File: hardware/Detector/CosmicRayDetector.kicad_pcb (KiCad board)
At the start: 2 copper layers, 100 x 100 mm, 29 parts, among them J1 USB_B_Micro, J2 Conn_01x01_Female, J3 Conn_01x01_Female, J4 Conn_01x01_Female, J5 Conn_01x01_Female, J6 Conn_01x04, J7 Conn_01x02, U1 HEF4093B

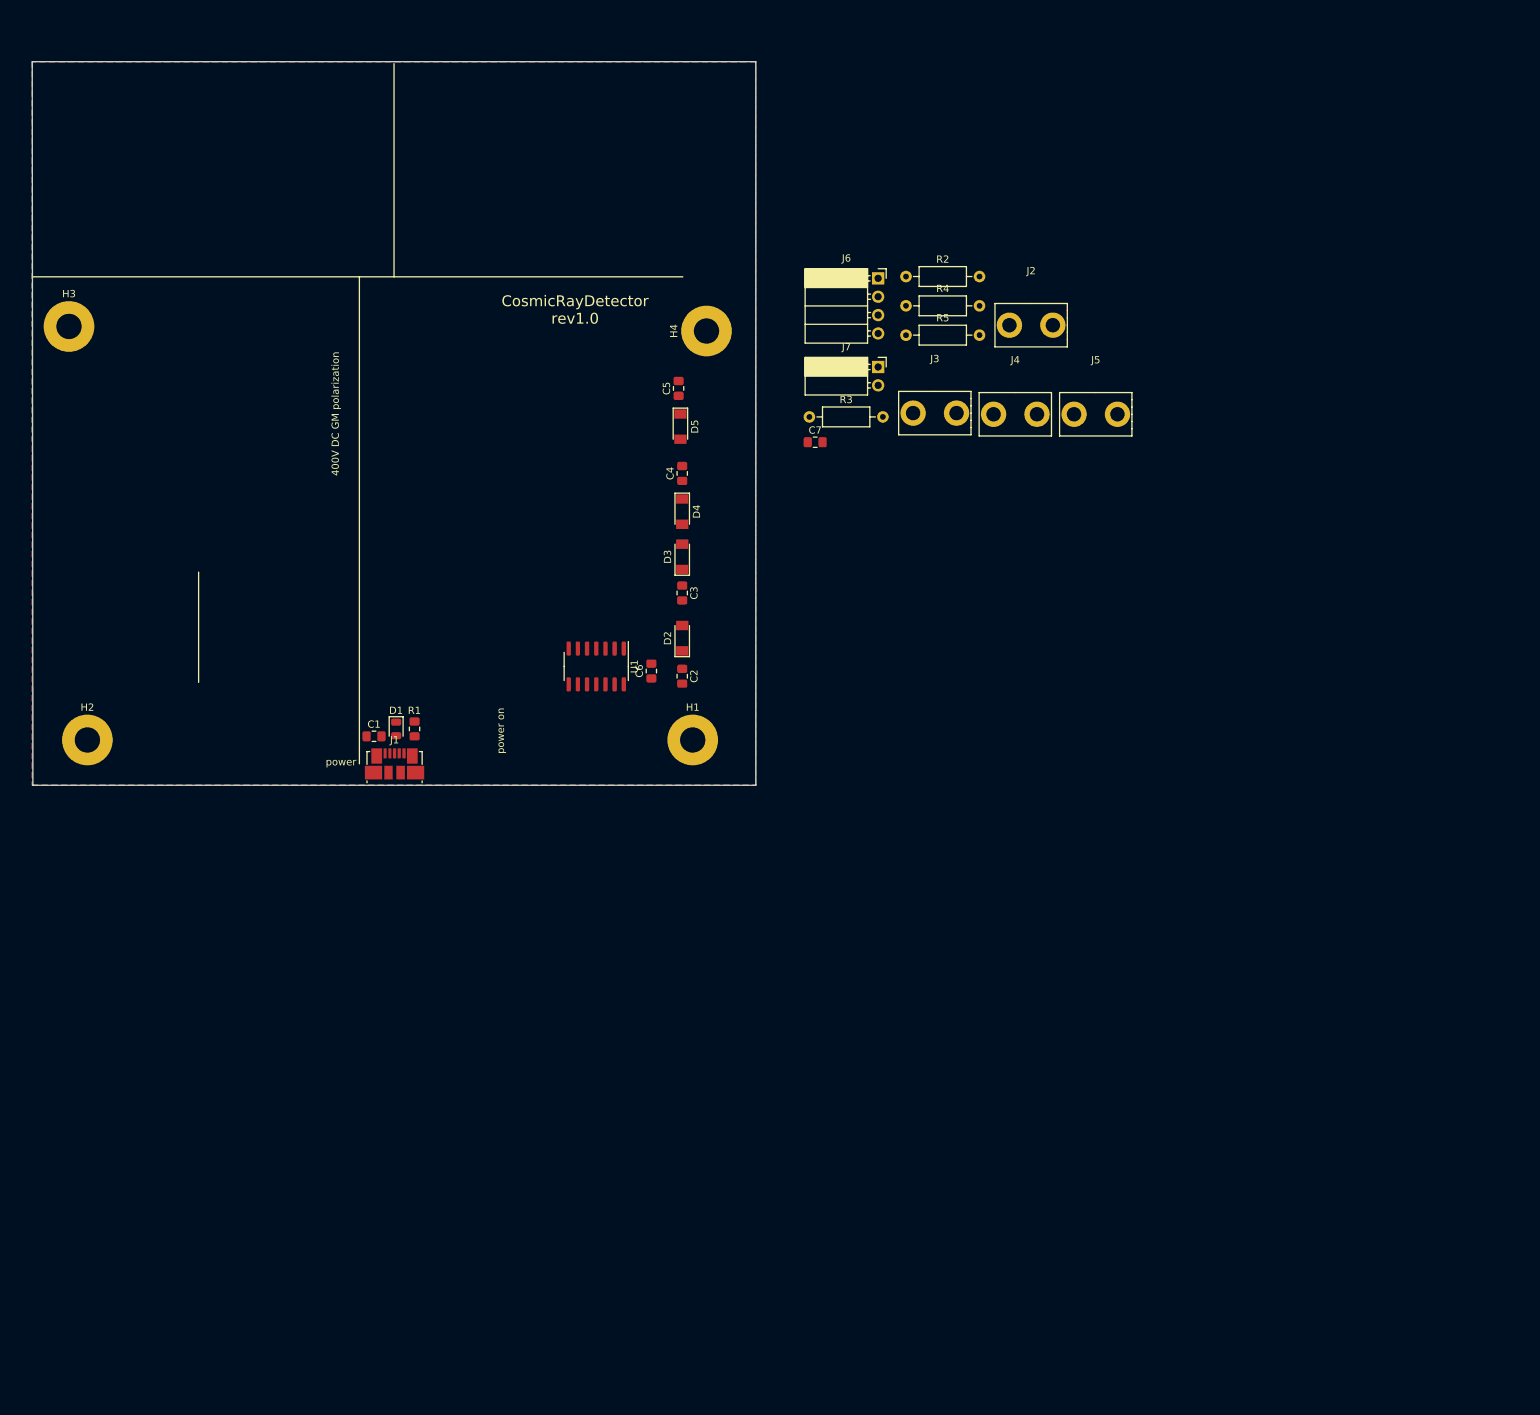
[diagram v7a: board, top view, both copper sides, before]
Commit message: pcb dimension and socket holes placement
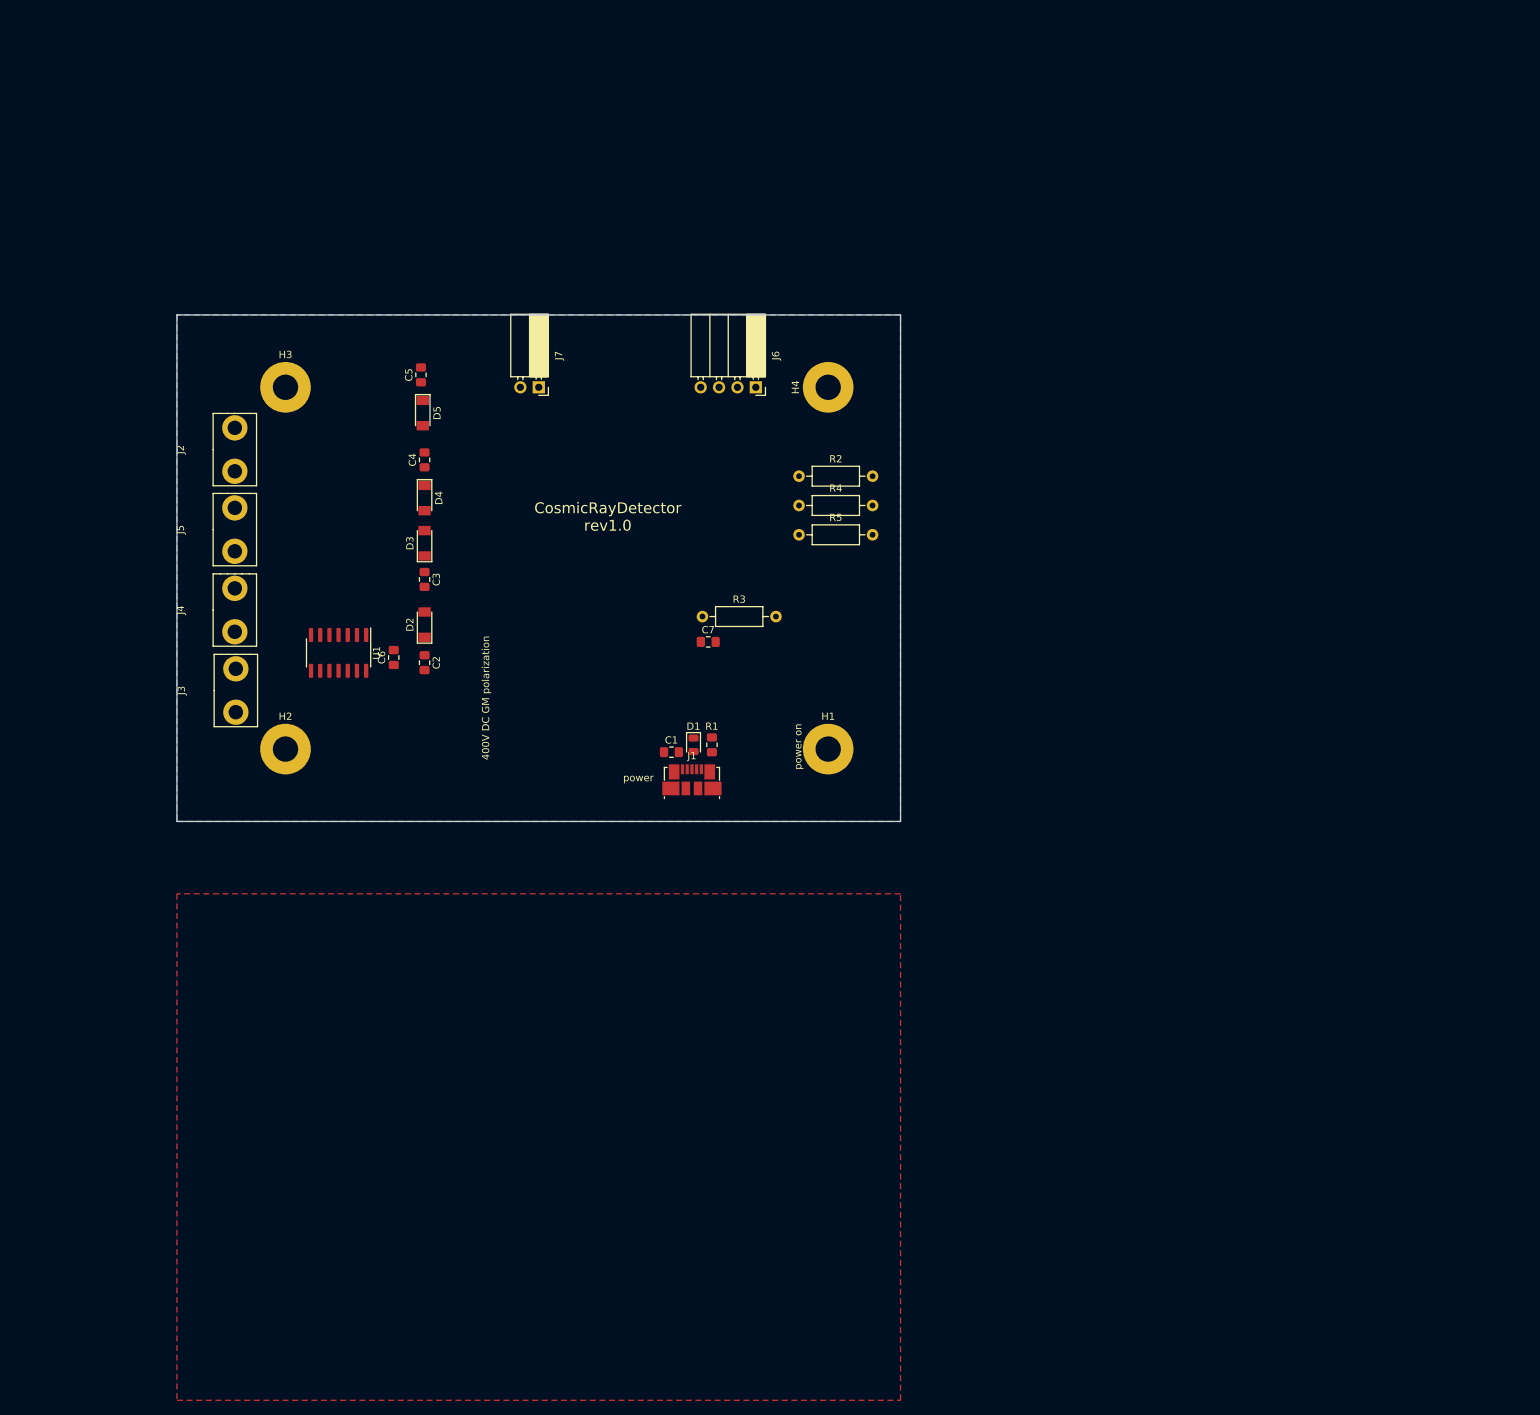
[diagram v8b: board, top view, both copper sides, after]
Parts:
- moved J5 129.2 mm to (20.0, 49.7), turned to 90 degrees
- moved J4 121.0 mm to (20.0, 60.8), turned to 90 degrees
- moved J2 120.7 mm to (20.0, 38.6), turned to 90 degrees
- moved J3 114.4 mm to (20.1, 71.9), turned to 90 degrees
- moved J7 47.0 mm to (70.0, 30.0), turned to 270 degrees
- moved R1 41.2 mm to (93.9, 79.4)
- moved C1 41.2 mm to (88.3, 80.4)
- moved D1 41.2 mm to (91.4, 79.4)
- moved J1 41.2 mm to (91.2, 84.2)
- moved C2 35.7 mm to (54.2, 68.1)
- moved C3 35.7 mm to (54.2, 56.6)
- moved C4 35.7 mm to (54.2, 40.0)
- moved C5 35.7 mm to (53.7, 28.3)
- moved D2 35.7 mm to (54.2, 62.8)
- moved D3 35.7 mm to (54.2, 51.6)
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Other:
- board size 100 x 100 mm -> 100 x 70 mm
